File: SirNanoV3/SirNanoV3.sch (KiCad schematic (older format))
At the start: 44 parts, among them J1 Conn_01x15, J2 Conn_01x15, J3 SirBlue, P1 USB_C_Plug_USB2.0, U1 ATmega328PB-MU, U2 SPX3819M5-L-3-3, U3 FT231XQ, Y1 20MHz

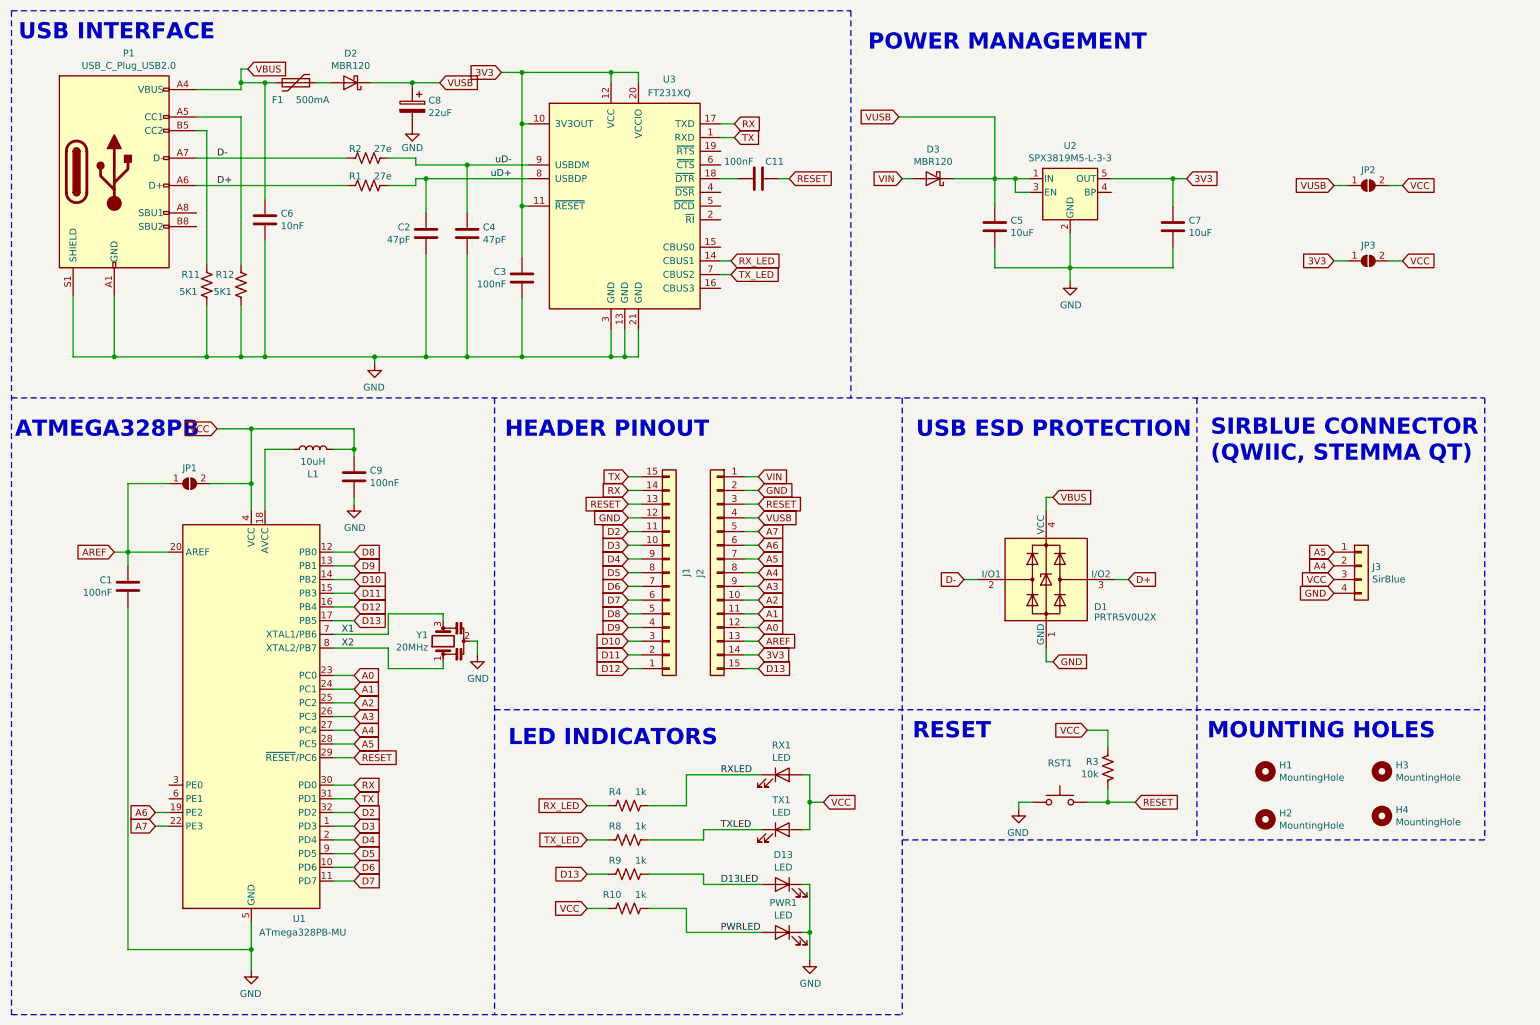
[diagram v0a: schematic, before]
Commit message: SirNanoR3 Update
20MHz Murata 3115 Resonator changed to 20MHz 3225_4P Resonator
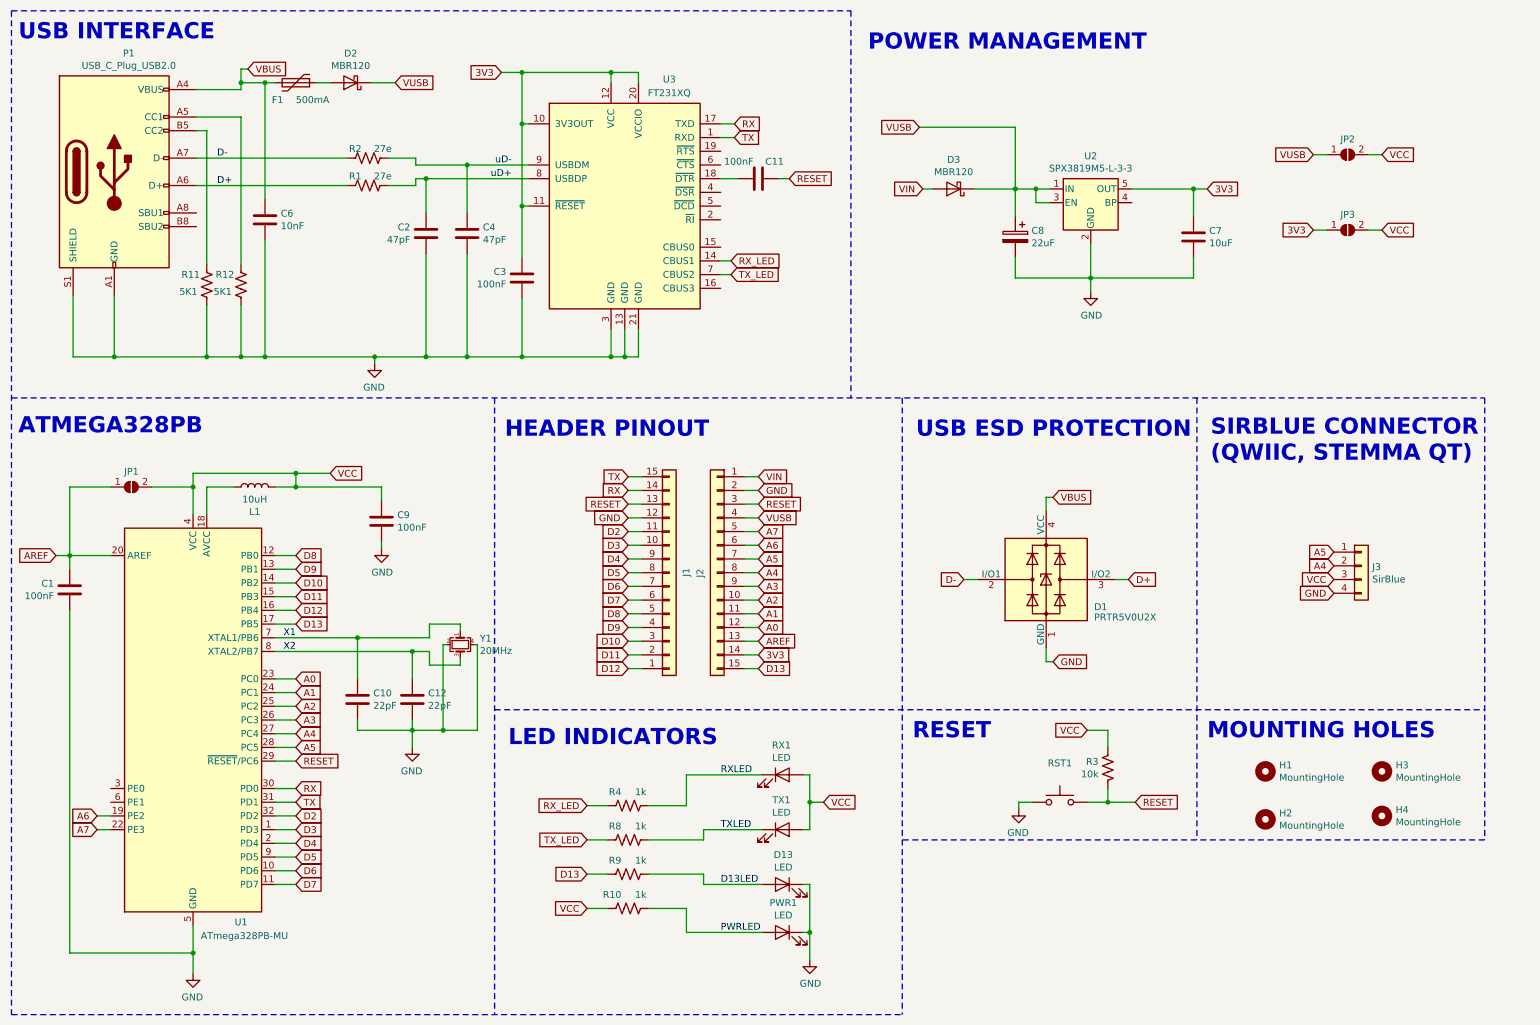
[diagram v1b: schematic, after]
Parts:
- removed C5: 10uF, Capacitor_SMD:C_0805_2012Metric, symbol Device:C
- removed Y1: 20MHz, Crystal:Resonator_SMD_muRata_CSTxExxV-3Pin_3.0x1.1mm, symbol Device:Resonator
- added C10, C12: 22pF, Capacitor_SMD:C_0603_1608Metric, symbol Device:C
- added Y1: 20MHz, Crystal:Crystal_SMD_3225-4Pin_3.2x2.5mm, symbol Device:Crystal_GND24_Small
- C1: Part C42998 -> C465158
- U2: Part (none) -> C9055
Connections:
- net GND: now also C10.2, C12.2, Y1.2, Y1.4
- net X1: now also C10.1, Y1.1
- net X2: now also C12.1, Y1.3
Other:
- moved on the sheet: C1, C7, C8, C9, D3, JP1, JP2, JP3, L1, U1, U2

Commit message: Revision3.1
Layout Improved, PE0 and PE1 used for SirBlue Connector + USB-C 3D Renders Added and Pictures Updated
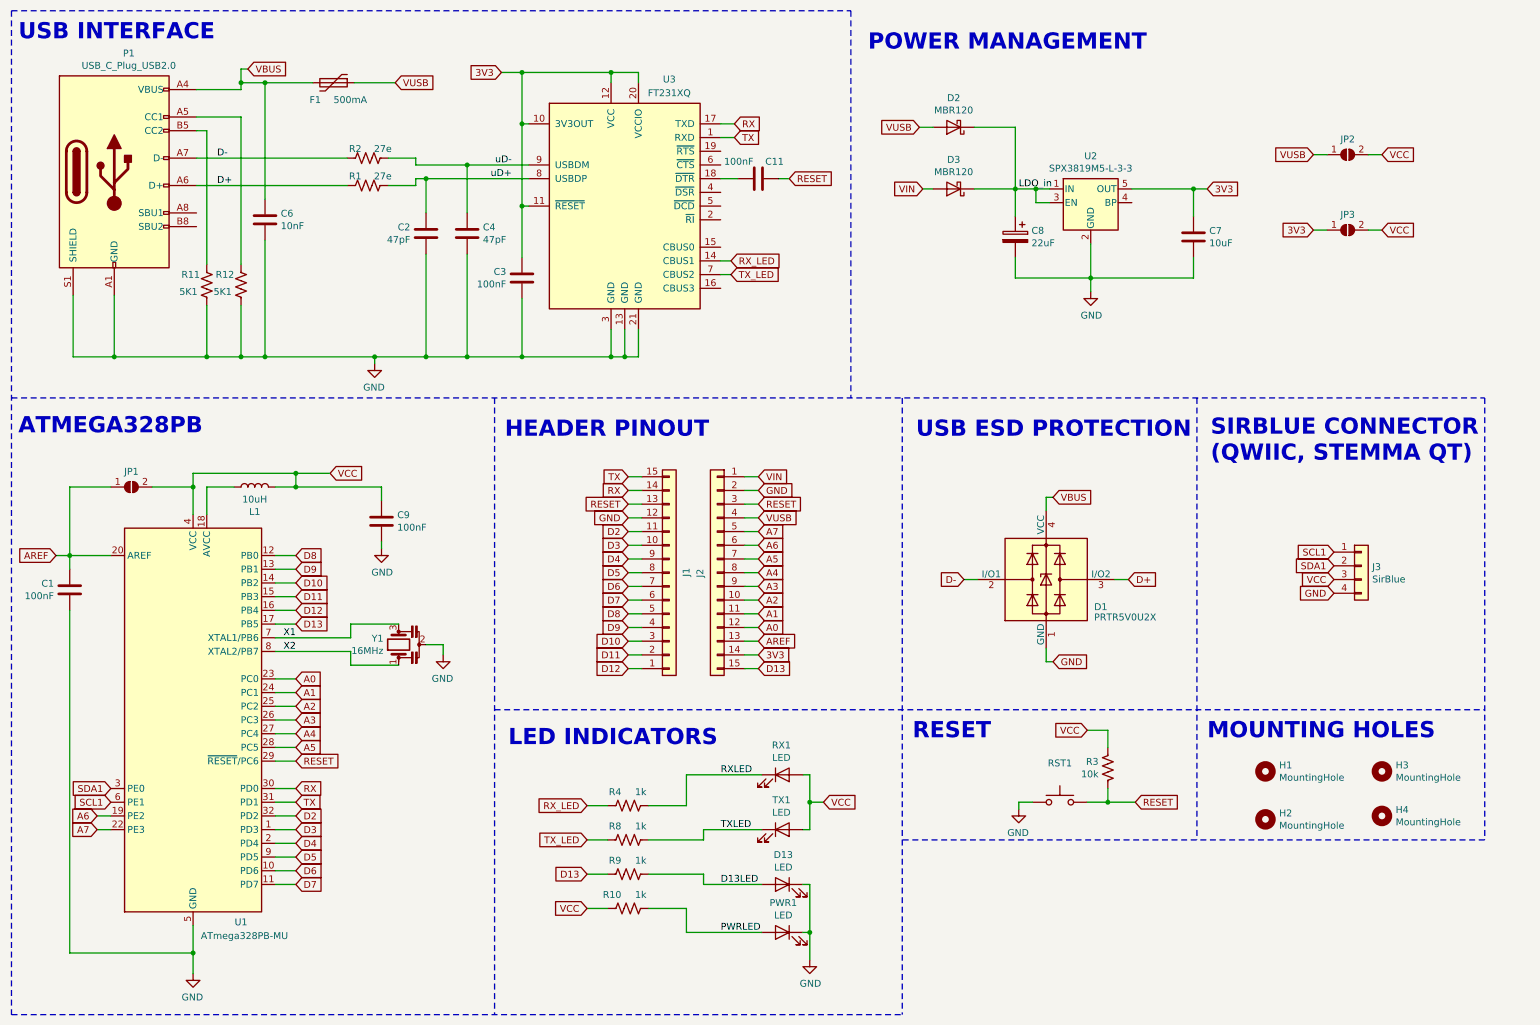
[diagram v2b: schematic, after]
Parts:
- removed C10, C12: 22pF, Capacitor_SMD:C_0603_1608Metric, symbol Device:C
- removed Y1: 20MHz, Crystal:Crystal_SMD_3225-4Pin_3.2x2.5mm, symbol Device:Crystal_GND24_Small
- added Y1: 16MHz, Crystal:Resonator_SMD_muRata_CSTxExxV-3Pin_3.0x1.1mm, symbol Device:Resonator
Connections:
- net A4: no longer J3.2 (Pin_2)
- net A5: no longer J3.1 (Pin_1)
- net GND: now also Y1.2
- net VUSB: now also D2.2 (A), F1.1; no longer C8.1, D2.1 (K), D3.1 (K), U2.1 (IN), U2.3 (EN)
- net X1: now also Y1.3
- net X2: now also Y1.1
- net SDA1: now reaches U1.3 (PE0)
- net SDA1: now also J3.2 (Pin_2)
- net SCL1: now reaches U1.6 (PE1)
- net SCL1: now also J3.1 (Pin_1)
- new net LDO_in: C8.1, D2.1 (K), D3.1 (K), U2.1 (IN), U2.3 (EN)
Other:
- moved on the sheet: D2, F1
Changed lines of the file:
@@
 Sheet 1 1
 Title "SirNano"
-Date "2020-03-02"
-Rev "3"
+Date "2020-04-11"
+Rev "3.1"
 Comp "SirBoard"
 Comment1 "www.SirBoard.com"
@@
 L Device:Polyfuse F1
 U 1 1 5D513147
-P 2550 1000
-F 0 "F1" V 2675 825 50  0000 L CNN
-F 1 "500mA" V 2675 1000 50  0000 L CNN
-F 2 "Resistor_SMD:R_0805_2012Metric" H 2600 800 50  0001 L CNN
-F 3 "~" H 2550 1000 50  0001 C CNN
-F 4 "C89657" H 2550 1000 50  0001 C CNN "Part"
-	1    2550 1000
+P 2825 1000
+F 0 "F1" V 2950 825 50  0000 L CNN
+F 1 "500mA" V 2950 1000 50  0000 L CNN
+F 2 "Resistor_SMD:R_0805_2012Metric" H 2875 800 50  0001 L CNN
+F 3 "~" H 2825 1000 50  0001 C CNN
+F 4 "C89657" H 2825 1000 50  0001 C CNN "Part"
+	1    2825 1000
 	0    1    1    0
 $EndComp
@@
 $EndComp
 Text GLabel 10125 4425 0    50   Input ~ 0
-A5
+SCL1
 Text GLabel 10125 4525 0    50   Input ~ 0
-A4
+SDA1
 Text GLabel 10125 4625 0    50   Input ~ 0
 VCC
@@
 L Device:D_Schottky D2
 U 1 1 5EA58C20
-P 2950 1000
-F 0 "D2" H 2950 786 50  0000 C CNN
-F 1 "MBR120" H 2950 876 50  0000 C CNN
-F 2 "Diode_SMD:D_SOD-123F" H 2950 1000 50  0001 C CNN
-F 3 "~" H 2950 1000 50  0001 C CNN
-F 4 "C223608" H 2950 1000 50  0001 C CNN "Part"
-	1    2950 1000
+P 7350 1325
+F 0 "D2" H 7350 1111 50  0000 C CNN
+F 1 "MBR120" H 7350 1201 50  0000 C CNN
+F 2 "Diode_SMD:D_SOD-123F" H 7350 1325 50  0001 C CNN
+F 3 "~" H 7350 1325 50  0001 C CNN
+F 4 "C223608" H 7350 1325 50  0001 C CNN "Part"
+	1    7350 1325
 	-1   0    0    1
 $EndComp
-Wire Wire Line
-	2700 1000 2800 1000
-Wire Wire Line
-	7100 1325 7800 1325
 Wire Wire Line
 	7800 1325 7800 1775
@@
 	2325 3000 3125 3000
 Wire Wire Line
-	2325 1000 2400 1000
+	2325 1000 2675 1000
 $Comp
 L Jumper:SolderJumper_2_Open JP3
@@
 $EndComp
 $Comp
-L Device:Crystal_GND24_Small Y1
-U 1 1 5E775976
-P 3750 5100
-F 0 "Y1" V 3705 5243 50  0000 L CNN
-F 1 "20MHz" V 3795 5243 50  0000 L CNN
-F 2 "Crystal:Crystal_SMD_3225-4Pin_3.2x2.5mm" H 3750 5100 50  0001 C CNN
-F 3 "https://datasheet.lcsc.com/szlcsc/2001061508_JGHC-S3220000181060_C479198.pdf" H 3750 5100 50  0001 C CNN
-F 4 "C479198" V 3750 5100 50  0001 C CNN "Part"
-	1    3750 5100
-	0    1    1    0
-$EndComp
-Wire Wire Line
-	3525 5050 3525 4950
-Wire Wire Line
-	3525 4950 3750 4950
-Wire Wire Line
-	3750 4950 3750 5000
-Wire Wire Line
-	3525 5150 3525 5250
-Wire Wire Line
-	3525 5250 3750 5250
-Wire Wire Line
-	3750 5250 3750 5200
-$Comp
 L power:GND #PWR0101
 U 1 1 5E7DEB03
-P 3400 5850
-F 0 "#PWR0101" H 3400 5600 50  0001 C CNN
-F 1 "GND" H 3405 5677 50  0000 C CNN
-F 2 "" H 3400 5850 50  0001 C CNN
-F 3 "" H 3400 5850 50  0001 C CNN
-	1    3400 5850
+P 3625 5175
+F 0 "#PWR0101" H 3625 4925 50  0001 C CNN
+F 1 "GND" H 3630 5002 50  0000 C CNN
+F 2 "" H 3625 5175 50  0001 C CNN
+F 3 "" H 3625 5175 50  0001 C CNN
+	1    3625 5175
 	-1   0    0    -1
 $EndComp
@@
 	-1   0    0    -1
 $EndComp
-$Comp
-L Device:C C10
-U 1 1 5E871F36
-P 3000 5500
-F 0 "C10" H 3115 5546 50  0000 L CNN
-F 1 "22pF" H 3115 5455 50  0000 L CNN
-F 2 "Capacitor_SMD:C_0603_1608Metric" H 3038 5350 50  0001 C CNN
-F 3 "~" H 3000 5500 50  0001 C CNN
-F 4 "C42998" H 3000 5500 50  0001 C CNN "Part"
-	1    3000 5500
-	1    0    0    -1
-$EndComp
-$Comp
-L Device:C C12
-U 1 1 5E8F1B5A
-P 3400 5500
-F 0 "C12" H 3515 5546 50  0000 L CNN
-F 1 "22pF" H 3515 5455 50  0000 L CNN
-F 2 "Capacitor_SMD:C_0603_1608Metric" H 3438 5350 50  0001 C CNN
-F 3 "~" H 3400 5500 50  0001 C CNN
-F 4 "C42998" H 3400 5500 50  0001 C CNN "Part"
-	1    3400 5500
-	1    0    0    -1
-$EndComp
-Wire Wire Line
-	2400 5050 3000 5050
-Wire Wire Line
-	2400 5150 3400 5150
-Wire Wire Line
-	3000 5350 3000 5050
-Connection ~ 3000 5050
-Wire Wire Line
-	3000 5050 3525 5050
-Wire Wire Line
-	3400 5350 3400 5150
-Connection ~ 3400 5150
-Wire Wire Line
-	3400 5150 3525 5150
-Wire Wire Line
-	3000 5650 3000 5725
-Wire Wire Line
-	3000 5725 3400 5725
-Wire Wire Line
-	3400 5725 3400 5650
-Wire Wire Line
-	3650 5100 3625 5100
-Wire Wire Line
-	3625 5100 3625 5725
-Wire Wire Line
-	3625 5725 3400 5725
-Connection ~ 3400 5725
-Wire Wire Line
-	3850 5100 3875 5100
-Wire Wire Line
-	3875 5100 3875 5725
-Wire Wire Line
-	3875 5725 3625 5725
-Connection ~ 3625 5725
-Wire Wire Line
-	3400 5850 3400 5725
 Wire Wire Line
 	1800 3850 2550 3850
@@
 Connection ~ 2550 3950
 Wire Wire Line
-	3100 1000 3275 1000
-Wire Wire Line
 	7800 2275 7800 2425
 Wire Wire Line
@@
 Wire Wire Line
 	7800 1975 7800 1775
+$Comp
+L Device:Resonator Y1
+U 1 1 5E95E86B
+P 3300 5100
+F 0 "Y1" V 3345 5211 50  0000 L CNN
+F 1 "16MHz" V 3255 5211 50  0000 L CNN
+F 2 "Crystal:Resonator_SMD_muRata_CSTxExxV-3Pin_3.0x1.1mm" H 3275 5100 50  0001 C CNN
+F 3 "~" H 3275 5100 50  0001 C CNN
+F 4 "C32180" V 3300 5100 50  0001 C CNN "Part"
+	1    3300 5100
+	0    -1   -1   0
+$EndComp
+Wire Wire Line
+	2400 5050 2950 5050
+Wire Wire Line
+	2950 5050 2950 4950
+Wire Wire Line
+	2950 4950 3300 4950
+Wire Wire Line
+	2400 5150 2950 5150
+Wire Wire Line
+	2950 5150 2950 5250
+Wire Wire Line
+	2950 5250 3300 5250
+Wire Wire Line
+	3500 5100 3625 5100
+Wire Wire Line
+	3625 5100 3625 5175
+Wire Wire Line
+	7100 1325 7200 1325
+Wire Wire Line
+	7500 1325 7800 1325
+Wire Wire Line
+	2975 1000 3275 1000
+Text Label 7825 1775 0    50   ~ 0
+LDO_in
+Text GLabel 1200 6250 0    50   Input ~ 0
+SCL1
+Text GLabel 1200 6150 0    50   Input ~ 0
+SDA1
 $EndSCHEMATC
